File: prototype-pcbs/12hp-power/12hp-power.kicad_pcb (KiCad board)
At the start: 2 copper layers, 58.4 x 109.2 mm, 892 parts, among them J1 IDC Header 2x8

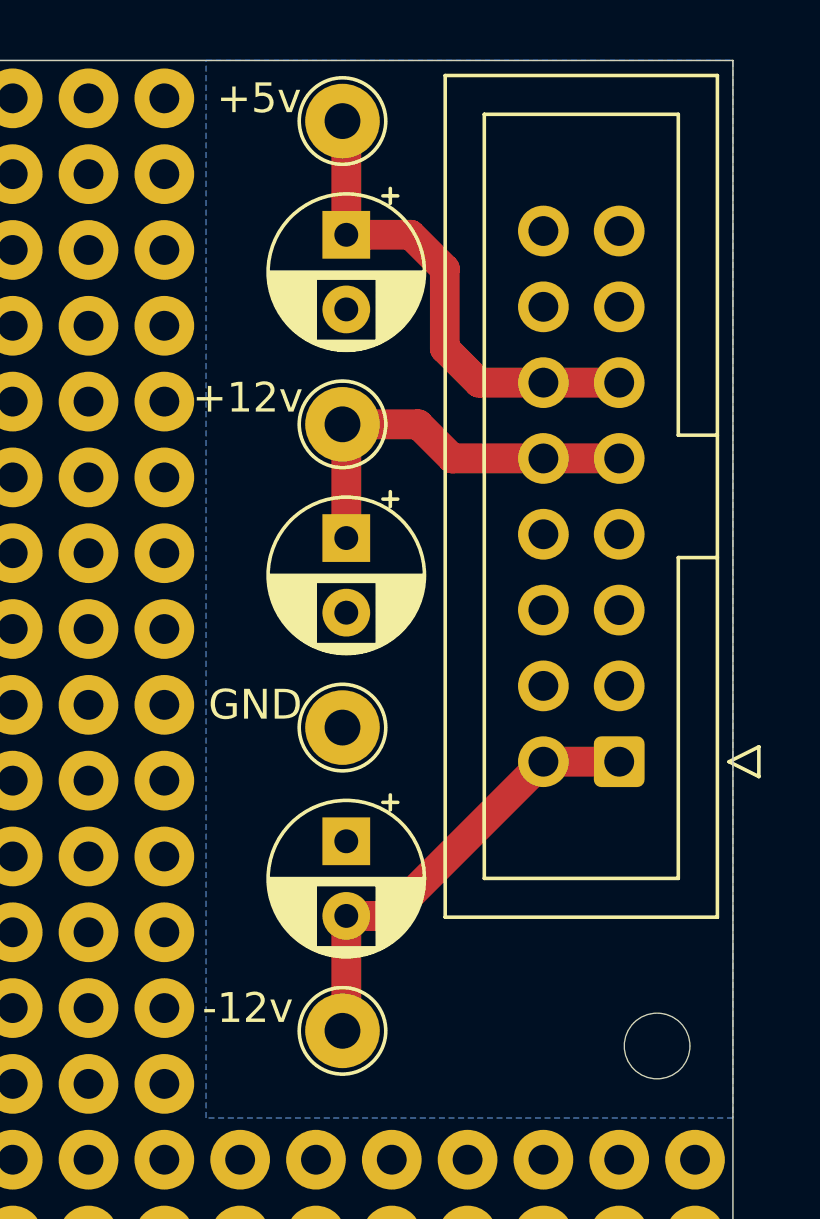
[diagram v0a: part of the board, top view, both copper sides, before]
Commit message: prototype-pcbs: added revision 2.1 for PCBs with Eurorack PSU connector.
gerber's silkscreen was missing the voltage references in the solder
points.
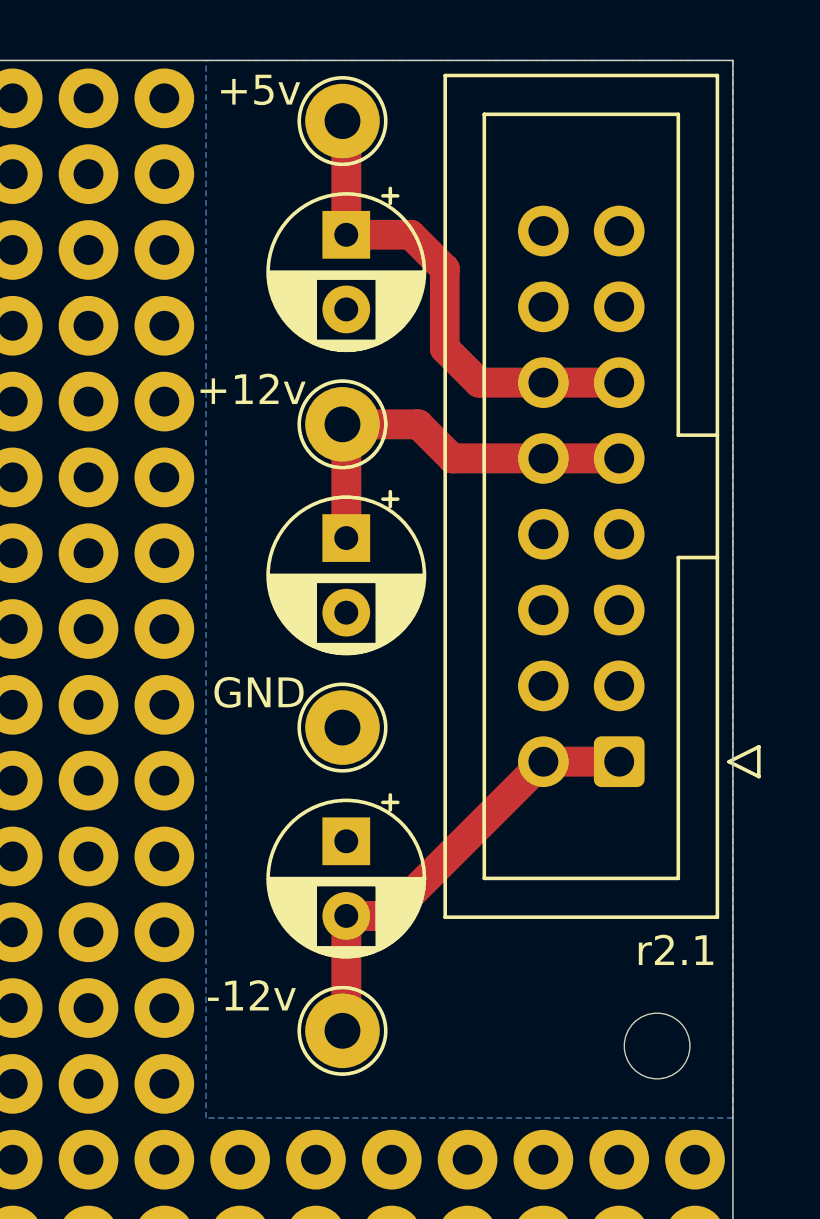
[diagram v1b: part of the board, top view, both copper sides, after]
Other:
- board text added: "r2.1"

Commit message: prototype-pcbs: 12hp-power: upgrade to kicad 6
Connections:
- J1 pad 13: (no net) -> unconnected-(J1-Pad13)
- J1 pad 14: (no net) -> unconnected-(J1-Pad14)
- J1 pad 15: (no net) -> unconnected-(J1-Pad15)
- J1 pad 16: (no net) -> unconnected-(J1-Pad16)
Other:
- net class Default removed
